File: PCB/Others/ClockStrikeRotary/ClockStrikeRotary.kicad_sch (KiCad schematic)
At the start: 21 parts, among them J1 In, J2 Out, J3 Port 1, J4 Port 2, SW1 Rotary_Encoder_Switch

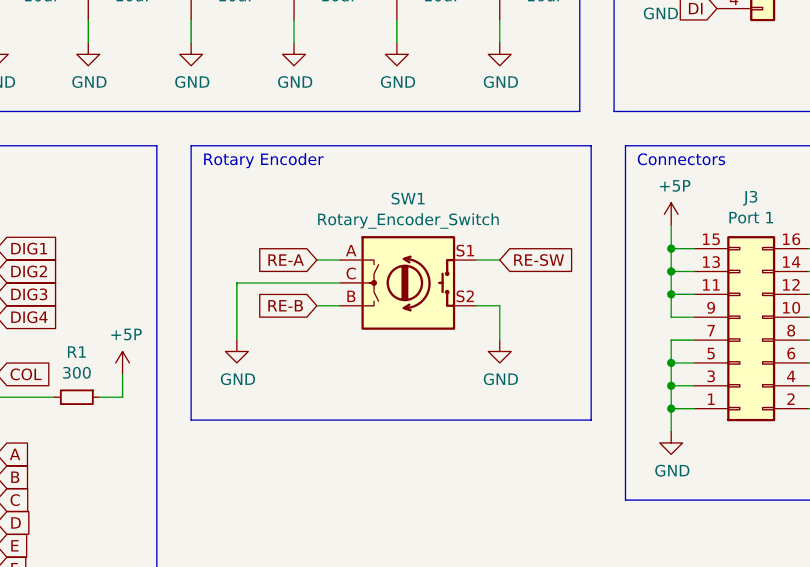
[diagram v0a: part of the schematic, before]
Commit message: Upgrade KiCad files from 6.0 to 7.0.
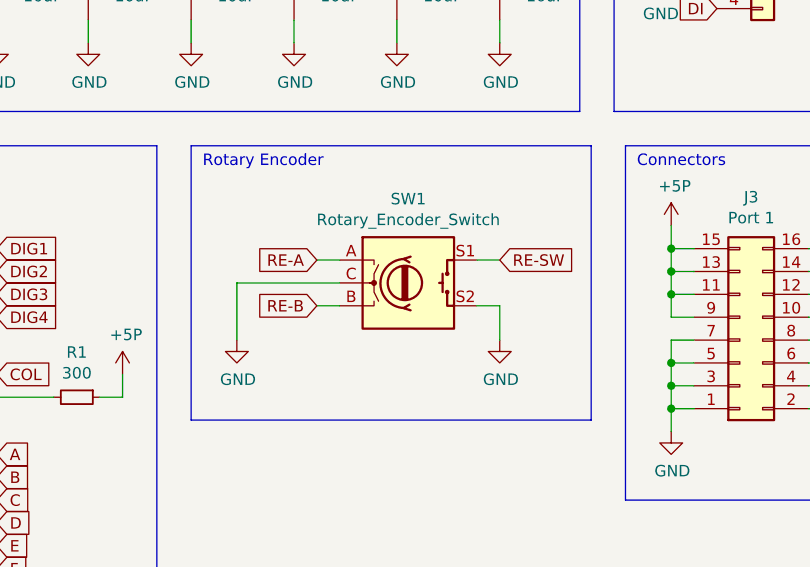
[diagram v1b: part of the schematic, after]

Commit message: First pass of PCB rework.
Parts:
- removed J2: Out, Connector_JST:JST_PH_B4B-PH-SM4-TB_1x04-1MP_P2.00mm_Vertical, symbol Connector_Generic:Conn_01x04
- removed J4: Port 2, Custom:PinHeader_2x08_P2.54mm_Vertical-Centered, symbol Connector_Generic:Conn_02x08_Odd_Even
- added C10, C8, C9: 4.7nF, Capacitor_SMD:C_0603_1608Metric, symbol Device:C_Small
- added C11: 10uF, Capacitor_SMD:C_0603_1608Metric, symbol Device:C_Small
- added C7: 0.1μF, Capacitor_SMD:C_0603_1608Metric, symbol Device:C_Small
- added H1, H2, H3, H4: MountingHole, MountingHole:MountingHole_3.2mm_M3, symbol Mechanical:MountingHole
- added J8: ICSP, Connector:Tag-Connect_TC2030-IDC-NL_2x03_P1.27mm_Vertical, symbol Connector_Generic:Conn_02x03_Odd_Even
- added R36, R37, R38: 10k, Resistor_SMD:R_0603_1608Metric, symbol Device:R_Small
- added R40, R41, R42, R43, R44, R45, R46, R47: 300, Resistor_SMD:R_0603_1608Metric, symbol Device:R_Small
- added R8: 47k, Resistor_SMD:R_0603_1608Metric, symbol Device:R_Small
- added U1: PIC18F15Q40, Package_SO:SSOP-20_5.3x7.2mm_P0.65mm, symbol KTANE:PIC18F15Q40
- C1, C2, C3, C4, C5, C6, C7: footprint Capacitor_SMD:C_0805_2012Metric -> Capacitor_SMD:C_0603_1608Metric; symbol Device:C -> Device:C_Small
- D8: footprint Display:ARK1136 -> KTANE:ARK1136
- J3: footprint Custom:PinHeader_2x08_P2.54mm_Vertical-Centered -> KTANE:PinHeader_2x08_P2.54mm_Vertical-Centered
- R1: footprint Resistor_SMD:R_0805_2012Metric -> Resistor_SMD:R_0603_1608Metric
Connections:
- net +5P: now also J3.2 (Pin_2); no longer J3.11 (Pin_11), J3.13 (Pin_13), J3.15 (Pin_15), J3.9 (Pin_9), R1.1
- net A: now also R40.1, U1.16 (RC0); no longer D8.13 (A), J3.14 (Pin_14)
- net B: now also R41.1, U1.14 (RC2); no longer D8.9 (B), J3.2 (Pin_2)
- net C: now also R42.1, U1.8 (RC6); no longer D8.4 (C), J3.6 (Pin_6)
- net COL: now also U1.3 (RA4)
- net D: now also R43.1, U1.6 (RC4); no longer D8.2 (D), J3.12 (Pin_12)
- net DP: now also R47.1, U1.7 (RC3); no longer D8.3 (DP), J3.8 (Pin_8)
- net E: now also R44.1, U1.5 (RC5); no longer D8.1 (E), J3.16 (Pin_16)
- net F: now also R45.1, U1.15 (RC1); no longer D8.12 (F), J3.10 (Pin_10)
- net G: now also R46.1, U1.9 (RC7); no longer D8.5 (G), J3.4 (Pin_4)
- net GND: now also J3.16 (Pin_16), C10.2, C11.2, C7.2, C8.2, C9.2, J8.3 (Pin_3), U1.20 (VSS); no longer J3.1 (Pin_1), J3.3 (Pin_3), J3.5 (Pin_5), J3.7 (Pin_7)
- net RE-A: now also J3.3 (Pin_3), C9.1, R37.2
- net RE-B: now also J3.1 (Pin_1), C10.1, R38.2
- net RE-SW: now also J3.5 (Pin_5), C8.1, R36.2
- net CO: no longer names the net of D7.5 (CO)
- net DO: no longer names the net of D7.6 (DO)
- new net: D8.1 (E), R44.2
- new net: D8.12 (F), R45.2
- new net: D8.13 (A), R40.2
- new net: D8.2 (D), R43.2
- new net: D8.3 (DP), R47.2
- new net: D8.4 (C), R42.2
- new net: D8.5 (G), R46.2
- new net: D8.9 (B), R41.2
- new net +3.3V: C11.1, J3.4 (Pin_4), J8.2 (Pin_2), R1.1, R36.1, R37.1, R38.1, R8.1, U1.1 (VDD)
- new net DIG-1: U1.11 (RB6)
- new net DIG-2: U1.12 (RB5)
- new net DIG-3: U1.13 (RB4)
- new net DIG-4: U1.10 (RB7)
- new net I2C-CLK: J3.6 (Pin_6)
- new net I2C-DAT: J3.8 (Pin_8)
- new net ICSPCLK: J3.10 (Pin_10), J8.5 (Pin_5), U1.18 (ISCPCLK/RA1)
- new net ICSPDAT: J3.12 (Pin_12), J8.4 (Pin_4), U1.19 (ICSPDAT/RA0)
- new net SPI-CIPO: J3.14 (Pin_14)
- new net SPI-CS: J3.15 (Pin_15), U1.2 (RA5)
- new net ~{MCLR}: C7.1, J8.1 (Pin_1), R8.2, U1.4 (~{MCLR/RA3})
- no-connect marks 0 -> 8
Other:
- added sheet CathodDriver (cathode_driver.kicad_sch)
- added sheet CathodDriver1 (cathode_driver.kicad_sch)
- added sheet CathodDriver2 (cathode_driver.kicad_sch)
- added sheet CathodDriver3 (cathode_driver.kicad_sch)
- note added: "Clock Cathode Drivers"
- note added: "Connector"
- note added: "In-Circuit Serial Programming"
- moved on the sheet: C1, C2, C3, C4, C5, C6, C7, D8, J1, J3, R1, SW1
